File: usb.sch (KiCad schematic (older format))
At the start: 34 parts, among them IC1 EP4CE10F17, P1 USB_A, U23 FT313HL-LQFP64-0.5, U25 TPS2024D, Y2 12MHz

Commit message: +5V routing
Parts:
- P1: symbol USB_A -> USB_A-RESCUE-Sputnik
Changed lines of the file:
@@
 EESchema Schematic File Version 2
+LIBS:Sputnik-rescue
 LIBS:sputnik
 LIBS:power
@@
 LIBS:Winbond
 LIBS:Sputnik-cache
-EELAYER 25 0
+EELAYER 26 0
 EELAYER END
 $Descr A4 11693 8268
@@
 VBUS
 $Comp
-L USB_A P1
+L USB_A-RESCUE-Sputnik P1
 U 1 1 588FD24C
 P 10500 3750
+AR Path="/588FD24C" Ref="P1"  Part="1"
+AR Path="/587F5FE1/588FD24C" Ref="P1"  Part="1"
 F 0 "P1" H 10700 3550 50  0000 C CNN
 F 1 "USB_A" H 10450 3950 50  0000 C CNN

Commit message: A bit of update
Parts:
- added R? (x6): 000, Resistors_SMD:R_0603, symbol R
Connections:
- net GND: now also R?.1, R?.1, R?.1
- net MSEL0: now also R?.1, R?.2
- net MSEL1: now also R?.1, R?.2
- net MSEL2: now also R?.1, R?.2

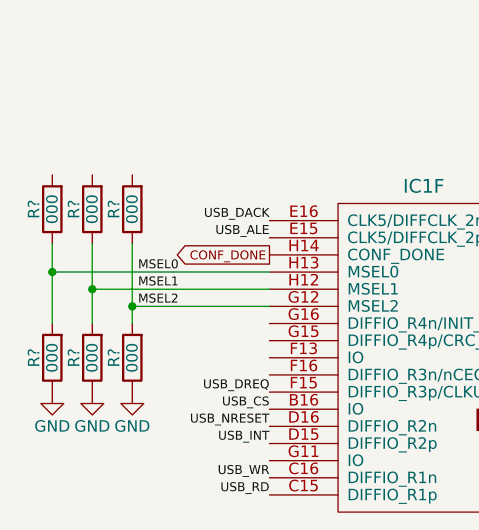
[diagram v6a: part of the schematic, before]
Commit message: VCCA and VCCD_PLL
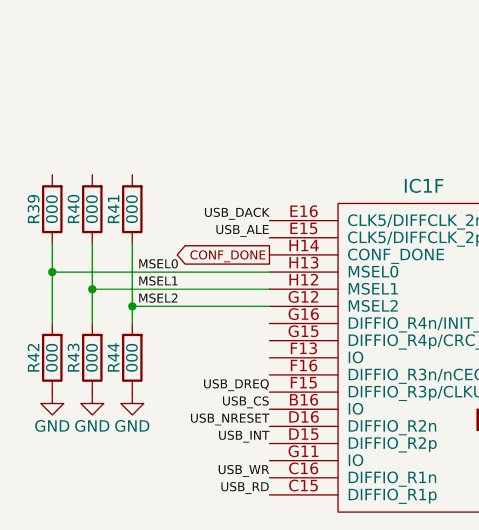
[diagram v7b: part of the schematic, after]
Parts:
- gave numbers to parts that had none: 6
